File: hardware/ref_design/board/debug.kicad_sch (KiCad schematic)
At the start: 8 parts, among them J5 SWD, J6 UART, SW18 BOOTSEL, SW19 RESET

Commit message: Reference design: case, board pipeline, routing tools and docs
- case/case.scad now owns every position the board needs (outline,
  cable slot, contacts, screws, USB-C, power button, pinholes, light
  pipes, height limits) and exports them to positions.json; tub, lid
  and power cap STLs, lens and board outlines as DXF.
- board/placement.py + tools/build_pcb.py: a 4-layer board built from
  KiCad's netlist with pcbnew, every footprint linked to its symbol
  (DRC schematic parity: 0), the RP2350B core's placement, routing and
  regulator copper copied from Raspberry Pi's minimal design.
- tools/route.py: planes, pre-routes the autorouter can't do (membrane
  combs, the display's grounded RGB pins, plane fan-out), Freerouting
  1.9 on a corrected copy of the board, pours, stitching, repair.
- Footprint copies that carry vendor 3D models (USB-C, JST, switches)
  checked against their pads; speaker pads moved to the back as SMD;
  the Alps switch's pads pulled back from its locating holes.
- docs: README, assembly, bring-up, pin map (generated), BOM, design
  review, and the Konnect problems met on the way.

Co-Authored-By: Claude Opus 5.5 (1M context) <noreply@anthropic.com>
Claude-Session: https://claude.ai/code/session_01KGgEu3CbFtCsvHRQgAFiCN
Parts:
- J5, J6: footprint Connector_JST:JST_SH_SM03B-SRSS-TB_1x03-1MP_P1.00mm_Horizontal -> battler:JST_SH_SM03B-SRSS-TB_1x03-1MP_P1.00mm_Horizontal
- SW18, SW19: footprint Button_Switch_SMD:SW_SPST_TS-1088-xR020 -> battler:SW_SPST_TS-1088-xR020
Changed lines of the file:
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@@
         (font
           (size 1.27 1.27))))
-    (property "Footprint" "Button_Switch_SMD:SW_SPST_TS-1088-xR020"
+    (property "Footprint" "battler:SW_SPST_TS-1088-xR020"
       (at 78.74 27.94 0)
       (effects
@@
         (font
           (size 1.27 1.27))))
-    (property "Footprint" "Button_Switch_SMD:SW_SPST_TS-1088-xR020"
+    (property "Footprint" "battler:SW_SPST_TS-1088-xR020"
       (at 144.78 27.94 0)
       (effects
@@
         (font
           (size 1.27 1.27))))
-    (property "Footprint" "Connector_JST:JST_SH_SM03B-SRSS-TB_1x03-1MP_P1.00mm_Horizontal"
+    (property "Footprint" "battler:JST_SH_SM03B-SRSS-TB_1x03-1MP_P1.00mm_Horizontal"
       (at 162.56 30.48 0)
       (effects
@@
         (font
           (size 1.27 1.27))))
-    (property "Footprint" "Connector_JST:JST_SH_SM03B-SRSS-TB_1x03-1MP_P1.00mm_Horizontal"
+    (property "Footprint" "battler:JST_SH_SM03B-SRSS-TB_1x03-1MP_P1.00mm_Horizontal"
       (at 185.42 30.48 0)
       (effects

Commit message: Reference design: board routed and DRC clean
- Core copy made faithful: Raspberry Pi's 0402 land patterns for the core
  passives (tools/lib_from_ref.py), their 3V3 stubs into the pour under the
  chip kept, and the uncopied-pad check made layer-aware (their board has a
  second flash footprint on the back, which had cost every QSPI track).
- TPS63001 re-placed and its power loop drawn by route.py as TI's layout
  guidance asks.
- tools/maze.py: a small A* router for the flash's SD2 line and for any
  connection Freerouting leaves open, with bounded rip-up.
- route.py: order-stable pre-routes (so --reuse is valid), fiducial
  keep-outs for the router, a second Freerouting pass when needed with a
  watchdog for its warning dialog, loose-copper cleanup.

check_pcb.py: 0 errors, 0 unconnected, 0 schematic parity issues.

Co-Authored-By: Claude Opus 5.5 (1M context) <noreply@anthropic.com>
Claude-Session: https://claude.ai/code/session_01KGgEu3CbFtCsvHRQgAFiCN
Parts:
- R25: footprint Resistor_SMD:R_0402_1005Metric -> battler:R_0402_1005Metric_RPi
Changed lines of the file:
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@@
         (font
           (size 1.27 1.27))))
-    (property "Footprint" "Resistor_SMD:R_0402_1005Metric"
+    (property "Footprint" "battler:R_0402_1005Metric_RPi"
       (at 35.56 27.94 0)
       (effects

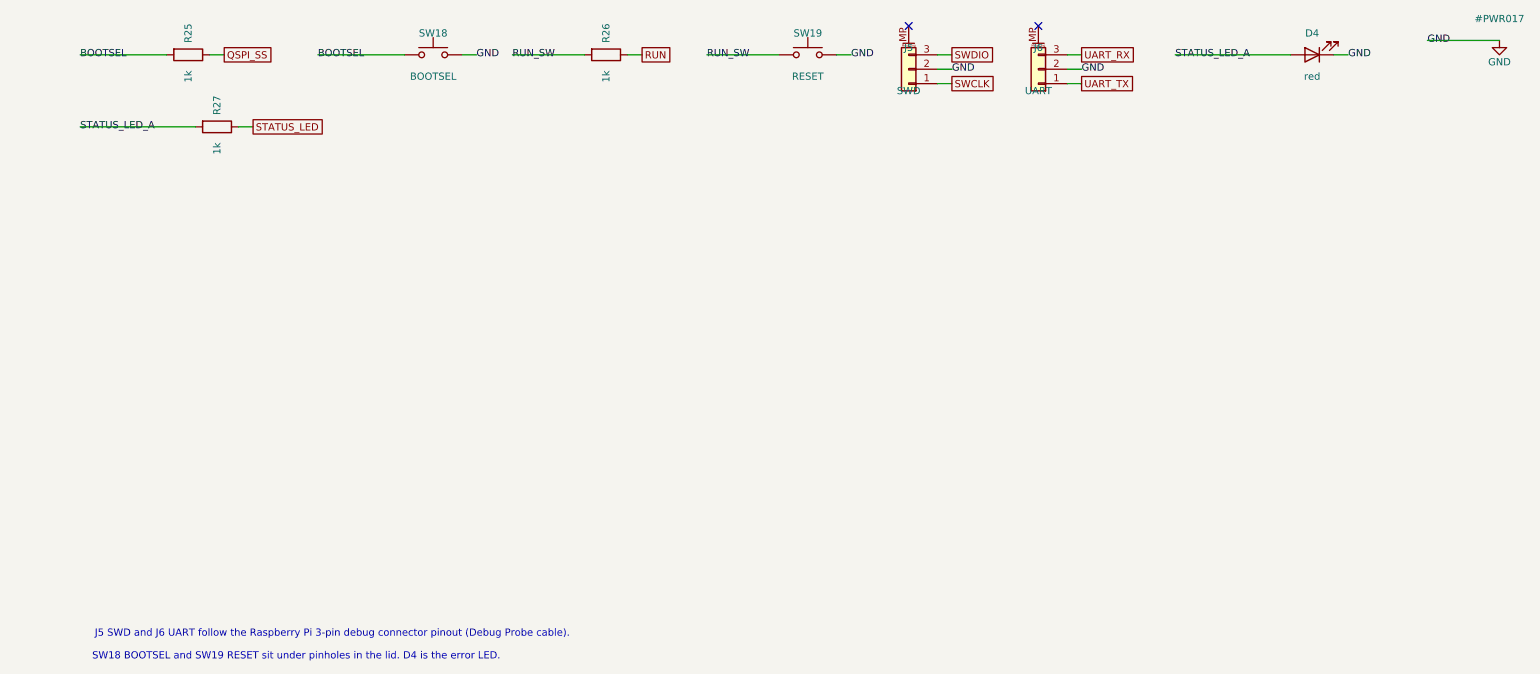
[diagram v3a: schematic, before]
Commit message: 2-layer fork: approved circuit changes in the design data and schematic
TP4056 charger (500 mA, TEMP grounded) with USB load sharing (B5819W, AO3401A
gate fed through a BAT54WS so it switches at once on an unplug, 22 uF on VSYS),
ME6211 3V3 LDO on the power latch, RP2354B with its flash inside (only the
QSPI_SS strap outside), 27 ohm 0603 USB resistors, SRV05-4 ESD, PWM audio
through two RC poles into an FM8002A, seat 1's Y contact as the power button,
no LEDs, no thermistor. Thermal-via footprints use 0.3 mm holes. Netlist
check passes, ERC 0 errors.

Co-Authored-By: Claude Opus 5.5 <noreply@anthropic.com>
Claude-Session: https://claude.ai/code/session_01KGgEu3CbFtCsvHRQgAFiCN
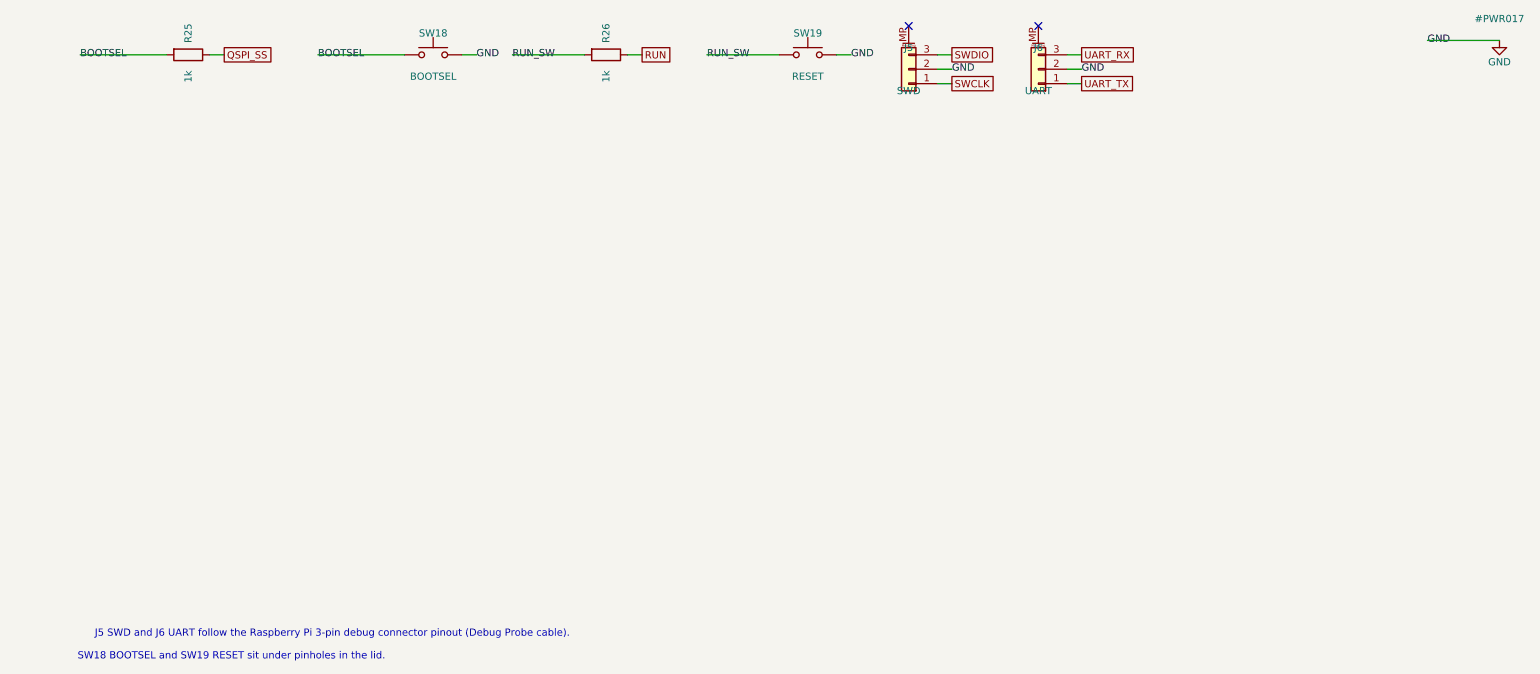
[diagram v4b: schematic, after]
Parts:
- removed D4: red, LED_SMD:LED_0603_1608Metric, symbol Device:LED
- removed R27: 1k, Resistor_SMD:R_0402_1005Metric, symbol Device:R
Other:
- note added: "SW18 BOOTSEL and SW19 RESET sit under pinholes in the lid."
- note removed: "SW18 BOOTSEL and SW19 RESET sit under pinholes in the lid. D4 is the error LED."
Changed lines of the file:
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@@
-  (wire
-    (pts
-      (xy 44.45 40.64)
-      (xy 46.99 40.64))
-)
-  (wire
-    (pts
-      (xy 36.83 40.64)
-      (xy 16.51 40.64))
-)
-  (wire
-    (pts
-      (xy 237.49 27.94)
-      (xy 240.03 27.94))
-)
-  (wire
-    (pts
-      (xy 229.87 27.94)
-      (xy 209.55 27.94))
-)
   (wire
     (pts
@@
         (size 1.27 1.27)))
 )
-  (text "SW18 BOOTSEL and SW19 RESET sit under pinholes in the lid. D4 is the error LED."
-    (at 54.61 134 0)
+  (text "SW18 BOOTSEL and SW19 RESET sit under pinholes in the lid."
+    (at 43.18 134 0)
     (effects
       (font
@@
     (at 193.04 30.48 0)
 )
-  (label "STATUS_LED_A"
-    (at 16.51 40.64 0)
-)
-  (label "GND"
-    (at 240.03 27.94 0)
-)
-  (label "STATUS_LED_A"
-    (at 209.55 27.94 0)
-)
   (label "GND"
     (at 254 25.4 0)
@@
     (shape passive)
     (at 193.04 33.02 0)
-)
-  (global_label "STATUS_LED"
-    (shape passive)
-    (at 46.99 40.64 0)
 )
   (symbol
@@
           (unit 1)))))
   (symbol
-    (lib_id "Device:R")
-    (at 40.64 40.64 270)
-    (unit 1)
-    (in_bom yes)
-    (on_board yes)
-    (dnp no)
-    (property "Reference" "R27"
-      (at 40.64 36.83 0)
-      (effects
-        (font
-          (size 1.27 1.27))))
-    (property "Value" "1k"
-      (at 40.64 44.45 0)
-      (effects
-        (font
-          (size 1.27 1.27))))
-    (property "Footprint" "Resistor_SMD:R_0402_1005Metric"
-      (at 40.64 40.64 0)
-      (effects
-        (font
-          (size 1.27 1.27))
-        (hide yes)))
-    (property "Datasheet" ""
-      (at 40.64 40.64 0)
-      (effects
-        (font
-          (size 1.27 1.27))
-        (hide yes)))
-    (property "LCSC" "C11702"
-      (at 0 0 0)
-      (effects
-        (font
-          (size 1.27 1.27))
-        (hide yes)))
-    (property "MPN" "0402WGF1001TCE"
-      (at 0 0 0)
-      (effects
-        (font
-          (size 1.27 1.27))
-        (hide yes)))
-    (property "Manufacturer" "UNI-ROYAL"
-      (at 0 0 0)
-      (effects
-        (font
-          (size 1.27 1.27))
-        (hide yes)))
-    (instances
-      (project ""
-        (path "/"
-          (reference "R27")
-          (unit 1)))))
-  (symbol
-    (lib_id "Device:LED")
-    (at 233.68 27.94 180)
-    (unit 1)
-    (in_bom yes)
-    (on_board yes)
-    (dnp no)
-    (property "Reference" "D4"
-      (at 233.68 24.13 0)
-      (effects
-        (font
-          (size 1.27 1.27))))
-    (property "Value" "red"
-      (at 233.68 31.75 0)
-      (effects
-        (font
-          (size 1.27 1.27))))
-    (property "Footprint" "LED_SMD:LED_0603_1608Metric"
-      (at 233.68 27.94 0)
-      (effects
-        (font
-          (size 1.27 1.27))
-        (hide yes)))
-    (property "Datasheet" ""
-      (at 233.68 27.94 0)
-      (effects
-        (font
-          (size 1.27 1.27))
-        (hide yes)))
-    (property "LCSC" "C2286"
-      (at 0 0 0)
-      (effects
-        (font
-          (size 1.27 1.27))
-        (hide yes)))
-    (property "MPN" "KT-0603R"
-      (at 0 0 0)
-      (effects
-        (font
-          (size 1.27 1.27))
-        (hide yes)))
-    (property "Manufacturer" "Hubei KENTO"
-      (at 0 0 0)
-      (effects
-        (font
-          (size 1.27 1.27))
-        (hide yes)))
-    (instances
-      (project ""
-        (path "/"
-          (reference "D4")
-          (unit 1)))))
-  (symbol
